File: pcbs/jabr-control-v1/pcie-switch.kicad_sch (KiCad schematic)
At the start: 24 parts, among them U303 PI7C9X2G304SL

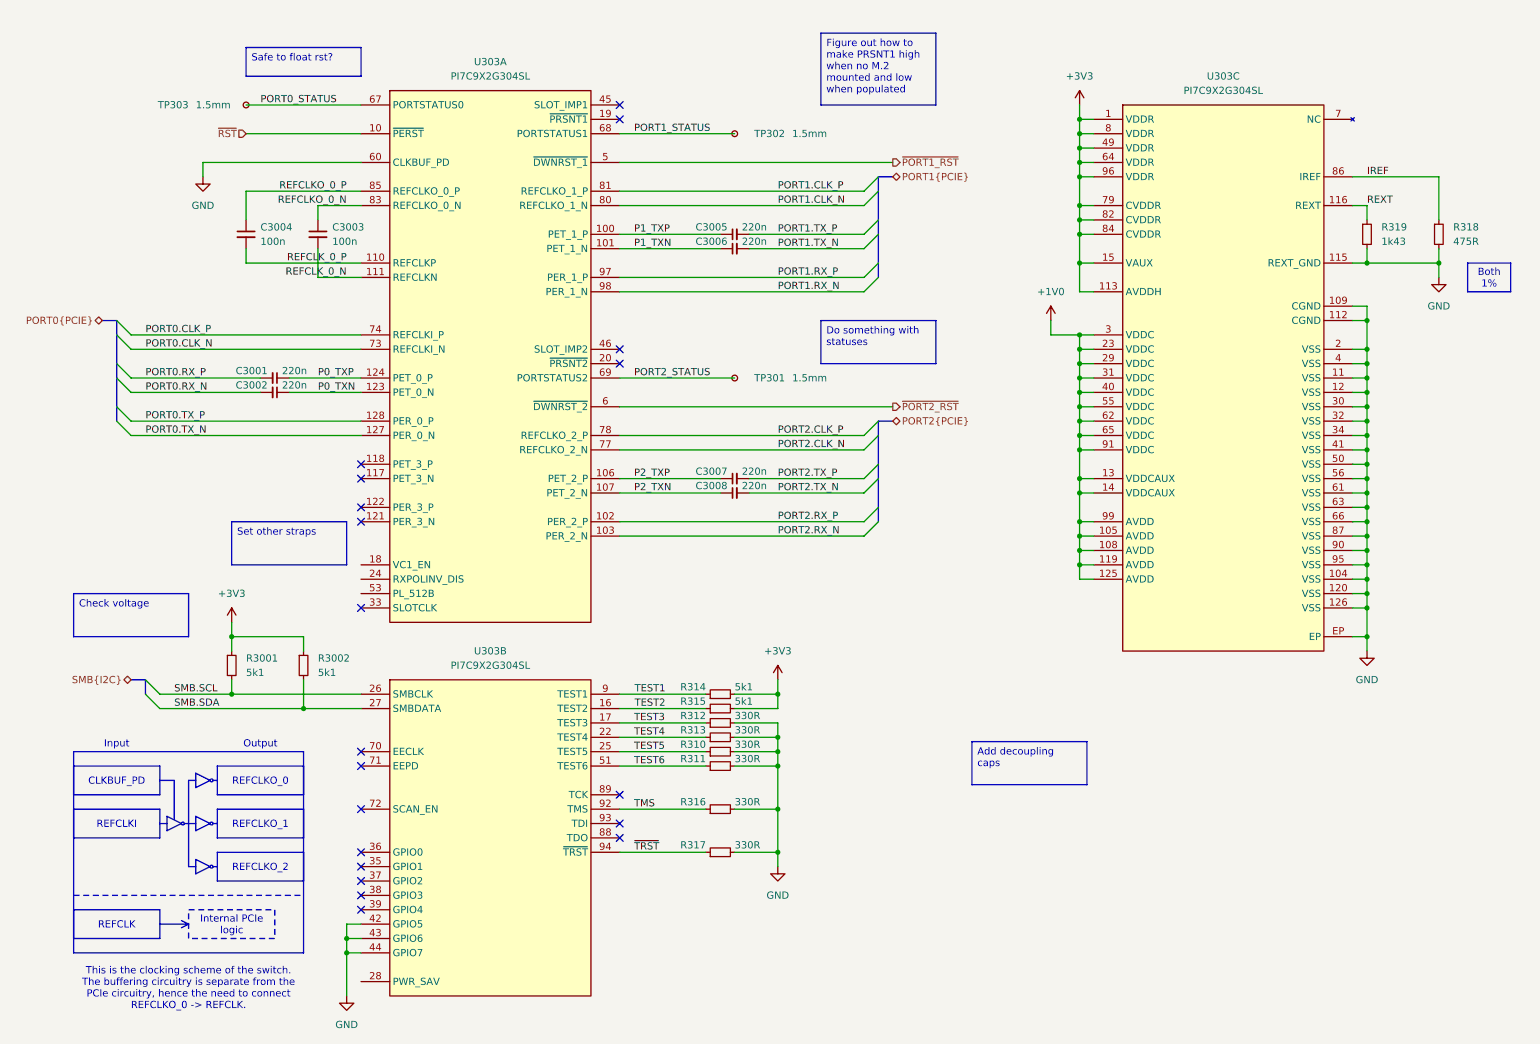
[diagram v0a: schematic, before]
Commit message: Schematic nearing completion, need to do GPIO and PHY decouplings caps
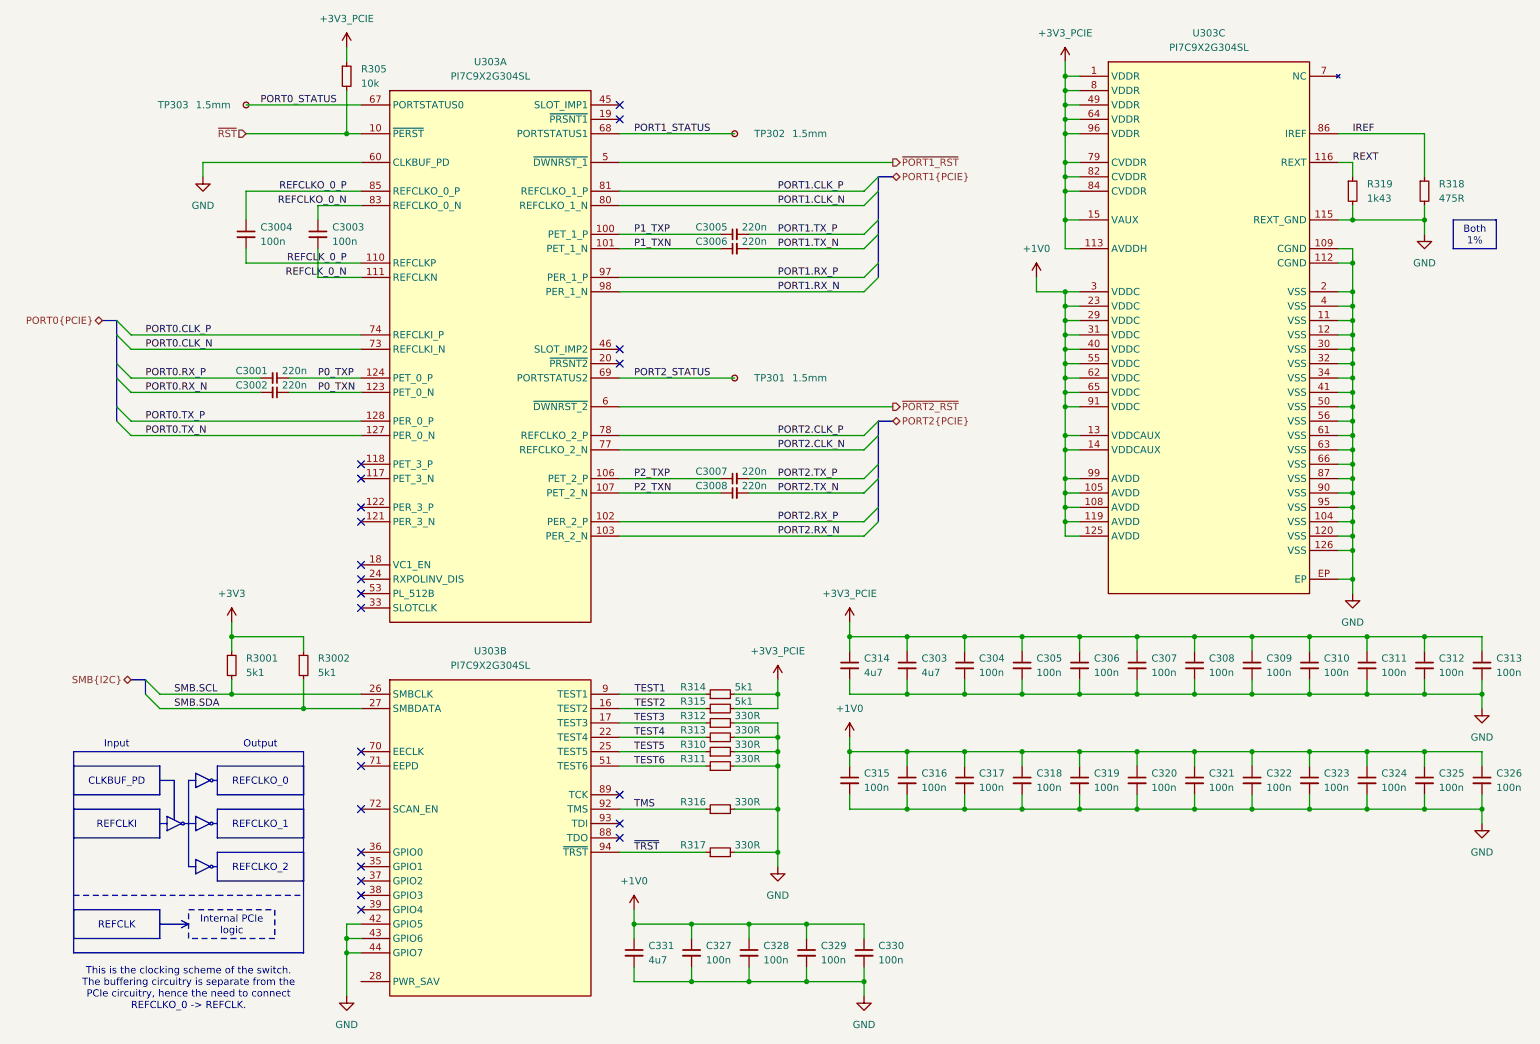
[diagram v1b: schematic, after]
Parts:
- added C303, C314, C331: 4u7, project_footprints:C_0402, symbol DEV:C_SMALL
- added C304, C305, C306, C307, C308, C309, C310, C311, C312, C313, C315, C316, C317, C318, C319, C320, C321, C322, C323, C324, C325, C326, C327, C328, C329, C330: 100n, project_footprints:C_0402, symbol DEV:C_SMALL
- added R305: 10k, project_footprints:R_0402, symbol DEV:R_SMALL
- TP301, TP302, TP303: footprint TestPoint:TestPoint_Pad_D1.5mm -> project_footprints:TestPoint_Pad_D1.5mm; now left out of the parts list
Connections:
- net +1V0: now also C315.1, C316.1, C317.1, C318.1, C319.1, C320.1, C321.1, C322.1, C323.1, C324.1, C325.1, C326.1, C327.1, C328.1, C329.1, C330.1, C331.1
- net +3V3: no longer R314.2, R315.2, U303.1 (VDDR), U303.113 (AVDDH), U303.15 (VAUX), U303.49 (VDDR), U303.64 (VDDR), U303.79 (CVDDR), U303.8 (VDDR), U303.82 (CVDDR), U303.84 (CVDDR), U303.96 (VDDR)
- net GND: now also C303.2, C304.2, C305.2, C306.2, C307.2, C308.2, C309.2, C310.2, C311.2, C312.2, C313.2, C314.2, C315.2, C316.2, C317.2, C318.2, C319.2, C320.2, C321.2, C322.2, C323.2, C324.2, C325.2, C326.2, C327.2, C328.2, C329.2, C330.2, C331.2
- net ~{RST}: now also R305.2
- new net +3V3_PCIE: C303.1, C304.1, C305.1, C306.1, C307.1, C308.1, C309.1, C310.1, C311.1, C312.1, C313.1, C314.1, R305.1, R314.2, R315.2, U303.1 (VDDR), U303.113 (AVDDH), U303.15 (VAUX), U303.49 (VDDR), U303.64 (VDDR), U303.79 (CVDDR), U303.8 (VDDR), U303.82 (CVDDR), U303.84 (CVDDR), U303.96 (VDDR)
- no-connect marks 20 -> 23
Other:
- moved on the sheet: R318, R319, U303C
